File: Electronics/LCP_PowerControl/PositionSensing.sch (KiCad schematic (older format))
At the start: 4 parts

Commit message: Aiming for rev 0.1 complete
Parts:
- RN3: renamed from RN?; footprint (none) -> Resistor_SMD:R_Array_Concave_2x0603; MPN (none) -> EXB-V4V472JV
- gave numbers to parts that had none: 3
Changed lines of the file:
@@
 Sheet 9 11
 Title ""
-Date ""
-Rev ""
+Date "2020-06-17"
+Rev "R0.1"
 Comp ""
-Comment1 ""
+Comment1 "Design by: Matt Casari"
 Comment2 ""
 Comment3 ""
@@
 P 7800 3500
 AR Path="/5EE2AA1B/5EE9B5F6" Ref="F?"  Part="1"
-AR Path="/5EE7B8CC/5EE9B5F6" Ref="F?"  Part="1"
-F 0 "F?" V 7700 3500 50  0000 C CNN
+AR Path="/5EE7B8CC/5EE9B5F6" Ref="F3"  Part="1"
+F 0 "F3" V 7700 3500 50  0000 C CNN
 F 1 "250mA" V 7850 3650 50  0000 C CNN
 F 2 "Fuse:Fuse_Bourns_MF-RG650" H 7850 3300 50  0001 L CNN
@@
 	8050 3650 8650 3650
 $Comp
-L power:+3V3 #PWR?
+L power:+3V3 #PWR061
 U 1 1 5EE9B7A7
 P 7450 3250
-F 0 "#PWR?" H 7450 3100 50  0001 C CNN
+F 0 "#PWR061" H 7450 3100 50  0001 C CNN
 F 1 "+3V3" H 7465 3423 50  0000 C CNN
 F 2 "" H 7450 3250 50  0001 C CNN
@@
 	7450 3500 7650 3500
 $Comp
-L power:GND #PWR?
+L power:GND #PWR062
 U 1 1 5EE9CB1B
 P 7450 4200
-F 0 "#PWR?" H 7450 3950 50  0001 C CNN
+F 0 "#PWR062" H 7450 3950 50  0001 C CNN
 F 1 "GND" H 7455 4027 50  0000 C CNN
 F 2 "" H 7450 4200 50  0001 C CNN
@@
 P 5100 3300
 AR Path="/5EE2A5A7/5EEF0BC5" Ref="RN?"  Part="1"
-AR Path="/5EE7B8CC/5EEF0BC5" Ref="RN?"  Part="1"
-F 0 "RN?" H 5188 3346 50  0000 L CNN
+AR Path="/5EE7B8CC/5EEF0BC5" Ref="RN3"  Part="1"
+F 0 "RN3" H 5188 3346 50  0000 L CNN
 F 1 "R_Pack02" H 5188 3255 50  0000 L CNN
-F 2 "" V 5275 3300 50  0001 C CNN
+F 2 "Resistor_SMD:R_Array_Concave_2x0603" V 5275 3300 50  0001 C CNN
 F 3 "~" H 5100 3300 50  0001 C CNN
+F 4 "EXB-V4V472JV" H 5100 3300 50  0001 C CNN "MPN"
 	1    5100 3300
 	1    0    0    -1
@@
 P 5000 2950
 AR Path="/5EE2A5A7/5EEF0BCB" Ref="#PWR?"  Part="1"
-AR Path="/5EE7B8CC/5EEF0BCB" Ref="#PWR?"  Part="1"
-F 0 "#PWR?" H 5000 2800 50  0001 C CNN
+AR Path="/5EE7B8CC/5EEF0BCB" Ref="#PWR060"  Part="1"
+F 0 "#PWR060" H 5000 2800 50  0001 C CNN
 F 1 "+3V3" H 5015 3123 50  0000 C CNN
 F 2 "" H 5000 2950 50  0001 C CNN
@@
 P 3650 3550
 AR Path="/5EE2AB43/5EEF683F" Ref="TP?"  Part="1"
-AR Path="/5EE7B8CC/5EEF683F" Ref="TP?"  Part="1"
-F 0 "TP?" H 3708 3668 50  0000 L CNN
+AR Path="/5EE7B8CC/5EEF683F" Ref="TP16"  Part="1"
+F 0 "TP16" H 3708 3668 50  0000 L CNN
 F 1 "TestPoint" H 3708 3577 50  0000 L CNN
 F 2 "TestPoint:TestPoint_Keystone_5000-5004_Miniature" H 3850 3550 50  0001 C CNN
@@
 P 4100 3550
 AR Path="/5EE2AB43/5EEF6EB6" Ref="TP?"  Part="1"
-AR Path="/5EE7B8CC/5EEF6EB6" Ref="TP?"  Part="1"
-F 0 "TP?" H 4158 3668 50  0000 L CNN
+AR Path="/5EE7B8CC/5EEF6EB6" Ref="TP17"  Part="1"
+F 0 "TP17" H 4158 3668 50  0000 L CNN
 F 1 "TestPoint" H 4158 3577 50  0000 L CNN
 F 2 "TestPoint:TestPoint_Keystone_5000-5004_Miniature" H 4300 3550 50  0001 C CNN

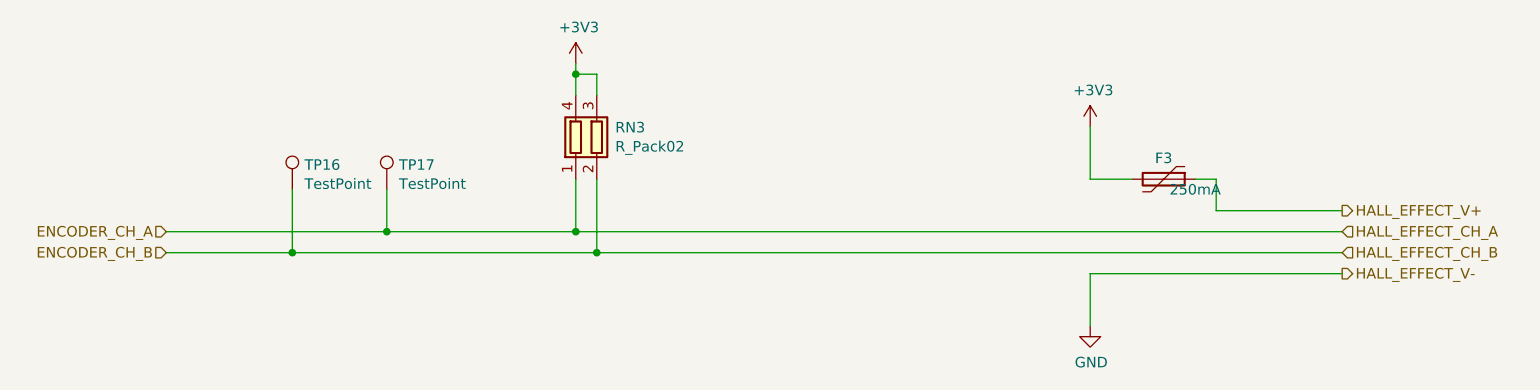
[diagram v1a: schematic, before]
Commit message: Rev1
Removed test points. Cleaned up unnecessary traces. Fixed electrical issues #1-#7
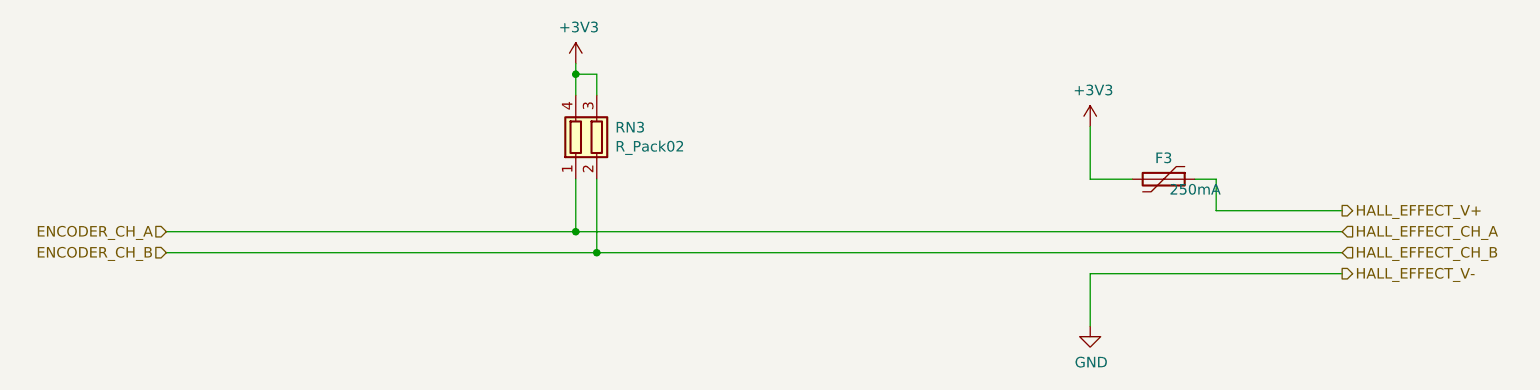
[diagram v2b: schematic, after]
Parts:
- removed TP16, TP17: TestPoint, TestPoint:TestPoint_Keystone_5000-5004_Miniature, symbol Connector:TestPoint
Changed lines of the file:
@@
 Text HLabel 3050 3850 0    50   Input ~ 0
 ENCODER_CH_B
-Wire Wire Line
-	3050 3850 3650 3850
 $Comp
 L Device:R_Pack02 RN?
@@
 Connection ~ 5000 3750
 Wire Wire Line
-	5000 3750 4100 3750
-Wire Wire Line
 	5100 3500 5100 3850
 Connection ~ 5100 3850
-$Comp
-L Connector:TestPoint TP?
-U 1 1 5EEF683F
-P 3650 3550
-AR Path="/5EE2AB43/5EEF683F" Ref="TP?"  Part="1"
-AR Path="/5EE7B8CC/5EEF683F" Ref="TP16"  Part="1"
-F 0 "TP16" H 3708 3668 50  0000 L CNN
-F 1 "TestPoint" H 3708 3577 50  0000 L CNN
-F 2 "TestPoint:TestPoint_Keystone_5000-5004_Miniature" H 3850 3550 50  0001 C CNN
-F 3 "~" H 3850 3550 50  0001 C CNN
-	1    3650 3550
-	1    0    0    -1
-$EndComp
-Wire Wire Line
-	3650 3550 3650 3850
-$Comp
-L Connector:TestPoint TP?
-U 1 1 5EEF6EB6
-P 4100 3550
-AR Path="/5EE2AB43/5EEF6EB6" Ref="TP?"  Part="1"
-AR Path="/5EE7B8CC/5EEF6EB6" Ref="TP17"  Part="1"
-F 0 "TP17" H 4158 3668 50  0000 L CNN
-F 1 "TestPoint" H 4158 3577 50  0000 L CNN
-F 2 "TestPoint:TestPoint_Keystone_5000-5004_Miniature" H 4300 3550 50  0001 C CNN
-F 3 "~" H 4300 3550 50  0001 C CNN
-	1    4100 3550
-	1    0    0    -1
-$EndComp
-Wire Wire Line
-	4100 3550 4100 3750
 Wire Wire Line
 	5000 3750 8650 3750
 Wire Wire Line
 	5100 3850 8650 3850
-Connection ~ 4100 3750
 Wire Wire Line
-	4100 3750 3050 3750
-Connection ~ 3650 3850
+	3050 3850 5100 3850
 Wire Wire Line
-	3650 3850 5100 3850
+	3050 3750 5000 3750
 $EndSCHEMATC

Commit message: BOM Update
Updated MPNs on components to match supplies as well as correcting some resistor values
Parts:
- F3: MPN MF-R065 -> MF-R025
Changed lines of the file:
@@
 F 2 "Fuse:Fuse_Bourns_MF-RG650" H 7850 3300 50  0001 L CNN
 F 3 "~" H 7800 3500 50  0001 C CNN
-F 4 "MF-R065" V 7800 3500 50  0001 C CNN "MPN"
+F 4 "MF-R025" V 7800 3500 50  0001 C CNN "MPN"
 	1    7800 3500
 	0    1    1    0

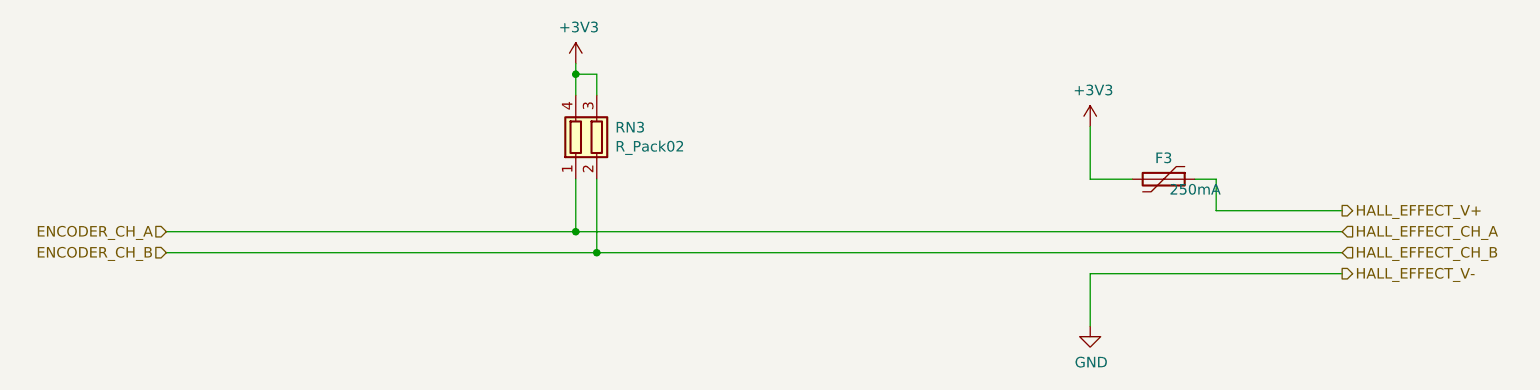
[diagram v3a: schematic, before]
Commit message: adding power control to pull-ups.
Adding ability to power on/off the pull-ups on the encoder
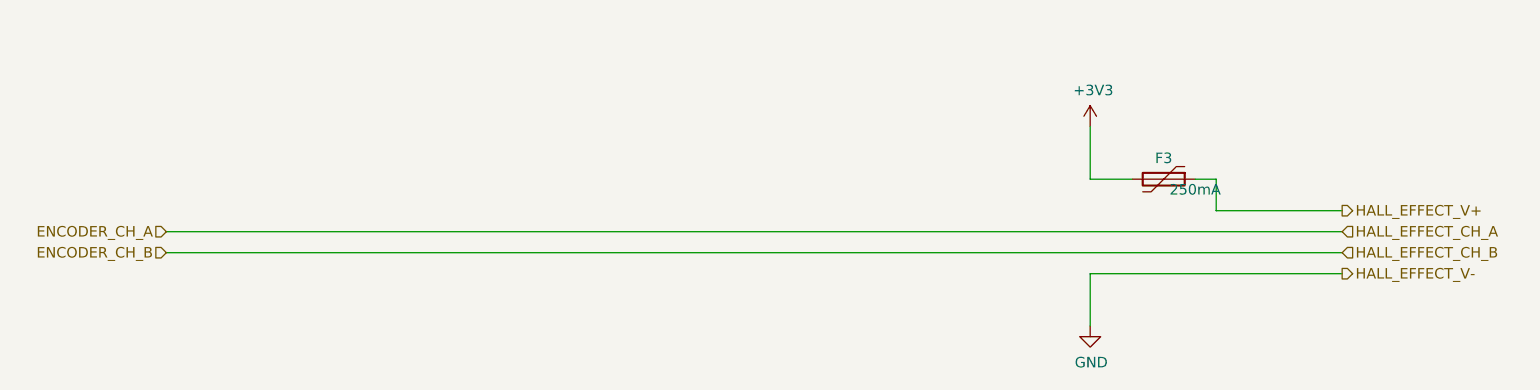
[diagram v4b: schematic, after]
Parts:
- removed RN3: R_Pack02, Resistor_SMD:R_Array_Concave_2x0603, symbol Device:R_Pack02
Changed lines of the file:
@@
 Text HLabel 3050 3850 0    50   Input ~ 0
 ENCODER_CH_B
-$Comp
-L Device:R_Pack02 RN?
-U 1 1 5EEF0BC5
-P 5100 3300
-AR Path="/5EE2A5A7/5EEF0BC5" Ref="RN?"  Part="1"
-AR Path="/5EE7B8CC/5EEF0BC5" Ref="RN3"  Part="1"
-F 0 "RN3" H 5188 3346 50  0000 L CNN
-F 1 "R_Pack02" H 5188 3255 50  0000 L CNN
-F 2 "Resistor_SMD:R_Array_Concave_2x0603" V 5275 3300 50  0001 C CNN
-F 3 "~" H 5100 3300 50  0001 C CNN
-F 4 "EXB-V4V472JV" H 5100 3300 50  0001 C CNN "MPN"
-	1    5100 3300
-	1    0    0    -1
-$EndComp
-$Comp
-L power:+3V3 #PWR?
-U 1 1 5EEF0BCB
-P 5000 2950
-AR Path="/5EE2A5A7/5EEF0BCB" Ref="#PWR?"  Part="1"
-AR Path="/5EE7B8CC/5EEF0BCB" Ref="#PWR060"  Part="1"
-F 0 "#PWR060" H 5000 2800 50  0001 C CNN
-F 1 "+3V3" H 5015 3123 50  0000 C CNN
-F 2 "" H 5000 2950 50  0001 C CNN
-F 3 "" H 5000 2950 50  0001 C CNN
-	1    5000 2950
-	1    0    0    -1
-$EndComp
 Wire Wire Line
-	5000 2950 5000 3000
+	3050 3750 8650 3750
 Wire Wire Line
-	5100 3100 5100 3000
-Wire Wire Line
-	5100 3000 5000 3000
-Connection ~ 5000 3000
-Wire Wire Line
-	5000 3000 5000 3100
-Wire Wire Line
-	5000 3500 5000 3750
-Connection ~ 5000 3750
-Wire Wire Line
-	5100 3500 5100 3850
-Connection ~ 5100 3850
-Wire Wire Line
-	5000 3750 8650 3750
-Wire Wire Line
-	5100 3850 8650 3850
-Wire Wire Line
-	3050 3850 5100 3850
-Wire Wire Line
-	3050 3750 5000 3750
+	3050 3850 8650 3850
 $EndSCHEMATC
